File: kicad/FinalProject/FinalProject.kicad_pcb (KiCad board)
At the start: 2 copper layers, 49.8 x 35.6 mm, 10 parts, among them IC1 MIC, U3 MPU-6050

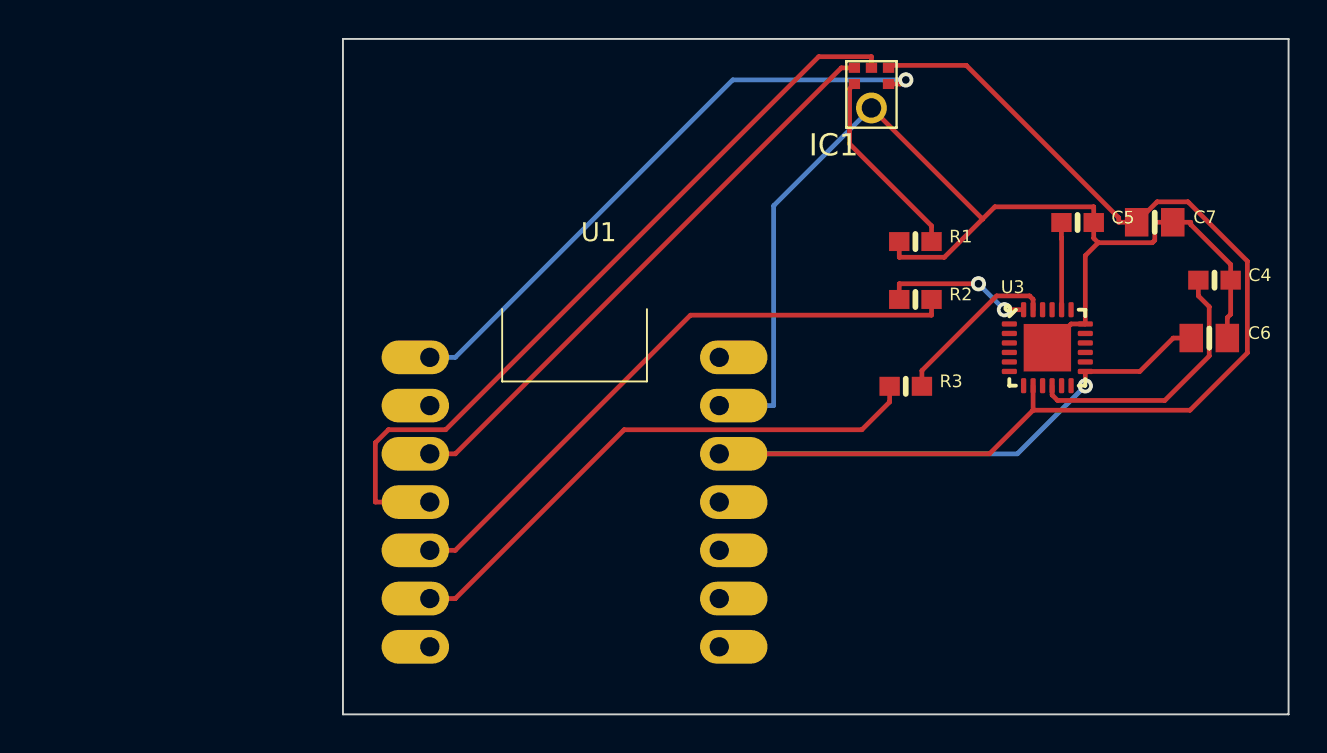
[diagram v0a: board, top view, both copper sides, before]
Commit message: added datasheets for led and stepper motor
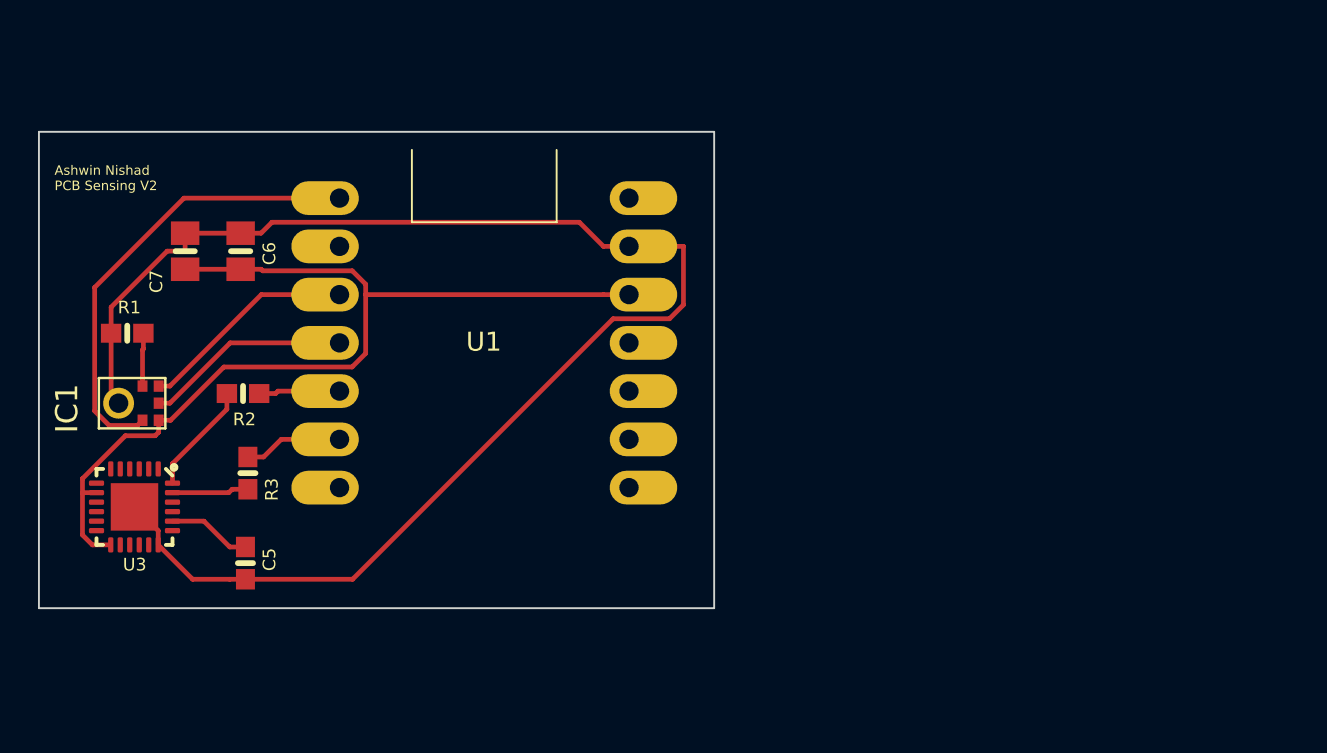
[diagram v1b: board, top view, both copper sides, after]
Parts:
- removed C4: 0.1uF, MPU6050:0603-NO
- moved C6 51.2 mm to (117.7, 96.3), turned to 90 degrees
- moved C7 51.1 mm to (114.8, 96.3), turned to 90 degrees
- moved U3 48.8 mm to (112.1, 109.7), turned to -90 degrees
- moved C5 47.3 mm to (118.0, 112.7), turned to -90 degrees
- moved IC1 42.2 mm to (112.0, 104.3), turned to -90 degrees
- moved R1 41.8 mm to (111.8, 100.6)
- moved R2 35.7 mm to (117.9, 103.8)
- moved R3 34.9 mm to (118.1, 108.0), turned to -90 degrees
- moved U1 9.64 mm to (130.6, 101.1)
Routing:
- net /3.3V: track 88.2 -> 50.8 mm, vias 1 -> 0
- net Net-(IC1-DATA): track 41.1 -> 10.8 mm
- net Net-(U1-GPIO4_A3_D3_SDA): track 32.4 -> 4.28 mm
- net Net-(U1-GPIO6_A5_D5_SCL): track 29.3 -> 5.21 mm
- net Net-(IC1-WS): track 30.8 -> 11.5 mm
- net GND: track 63.1 -> 78.3 mm
- net /REGOUT: track 14.1 -> 0.00 mm
- net Net-(IC1-BCLK): track 32.1 -> 24.3 mm, vias 1 -> 0
- net /SELECT: track 10.2 -> 2.80 mm
- net /SCL_3V: track 8.93 -> 4.04 mm
- net /SDA_3V: track 7.94 -> 5.91 mm, vias 2 -> 0
- net /CPOUT: track 5.01 -> 4.41 mm
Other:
- board size 49.8 x 35.6 mm -> 35.5 x 25.1 mm
- board text added: "Ashwin Nishad PCB Sensing V2"
